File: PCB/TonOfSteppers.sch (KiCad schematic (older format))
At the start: 14 parts, among them J1 PI To Board, J11 SW, J12 SW, J13 SW, J2 PiGPIO

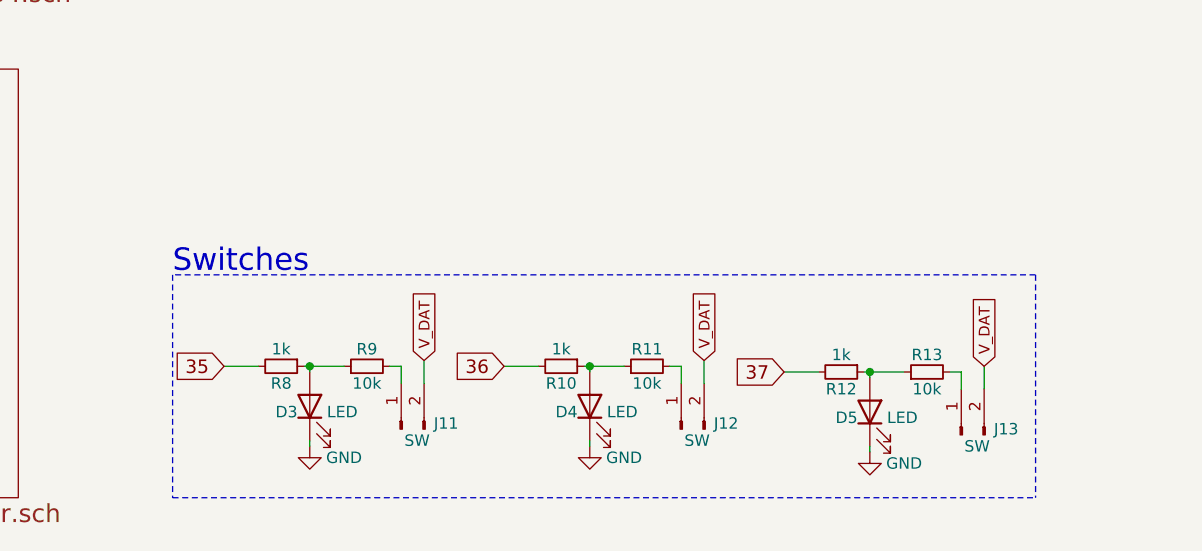
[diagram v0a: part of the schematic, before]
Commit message: TOS new version
-Added usb power for display.
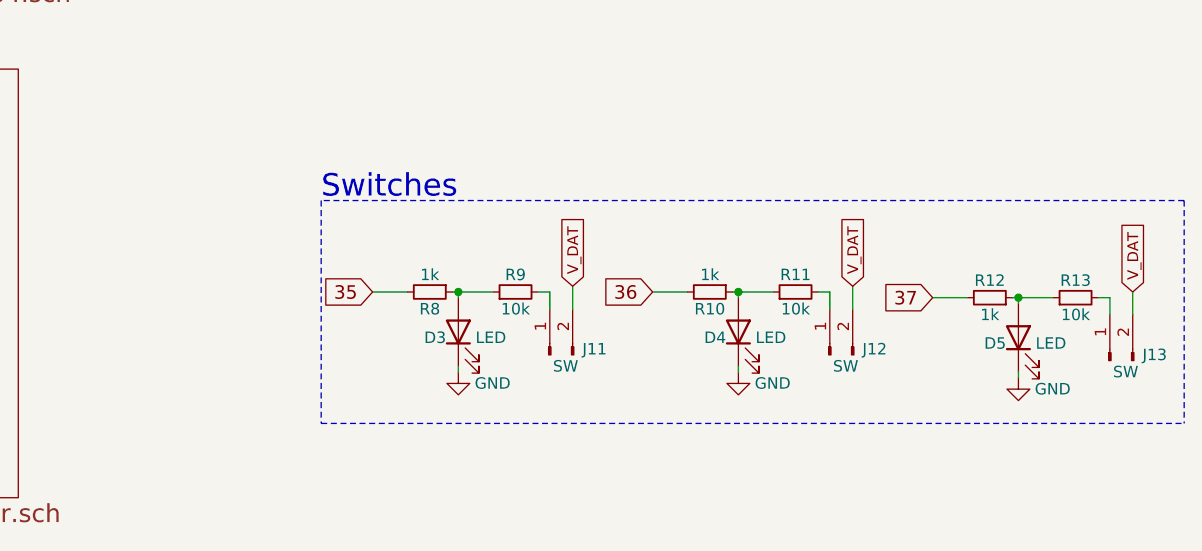
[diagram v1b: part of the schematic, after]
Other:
- moved on the sheet: D3, D4, D5, J11, J12, J13, R10, R11, R12, R13, R8, R9
